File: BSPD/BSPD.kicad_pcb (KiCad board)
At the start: 2 copper layers, 100.3 x 69.5 mm, 96 parts, among them Q1 BC548, Q2 BC548, Q3 BC548, Q4 BC548, Q5 BC548, Q6 BC557, Q7 BC548, SW1 SW_DPDT_x2, U1 TL431D, U2 LM358, U3 LM358, U5 LM358, U6 4001

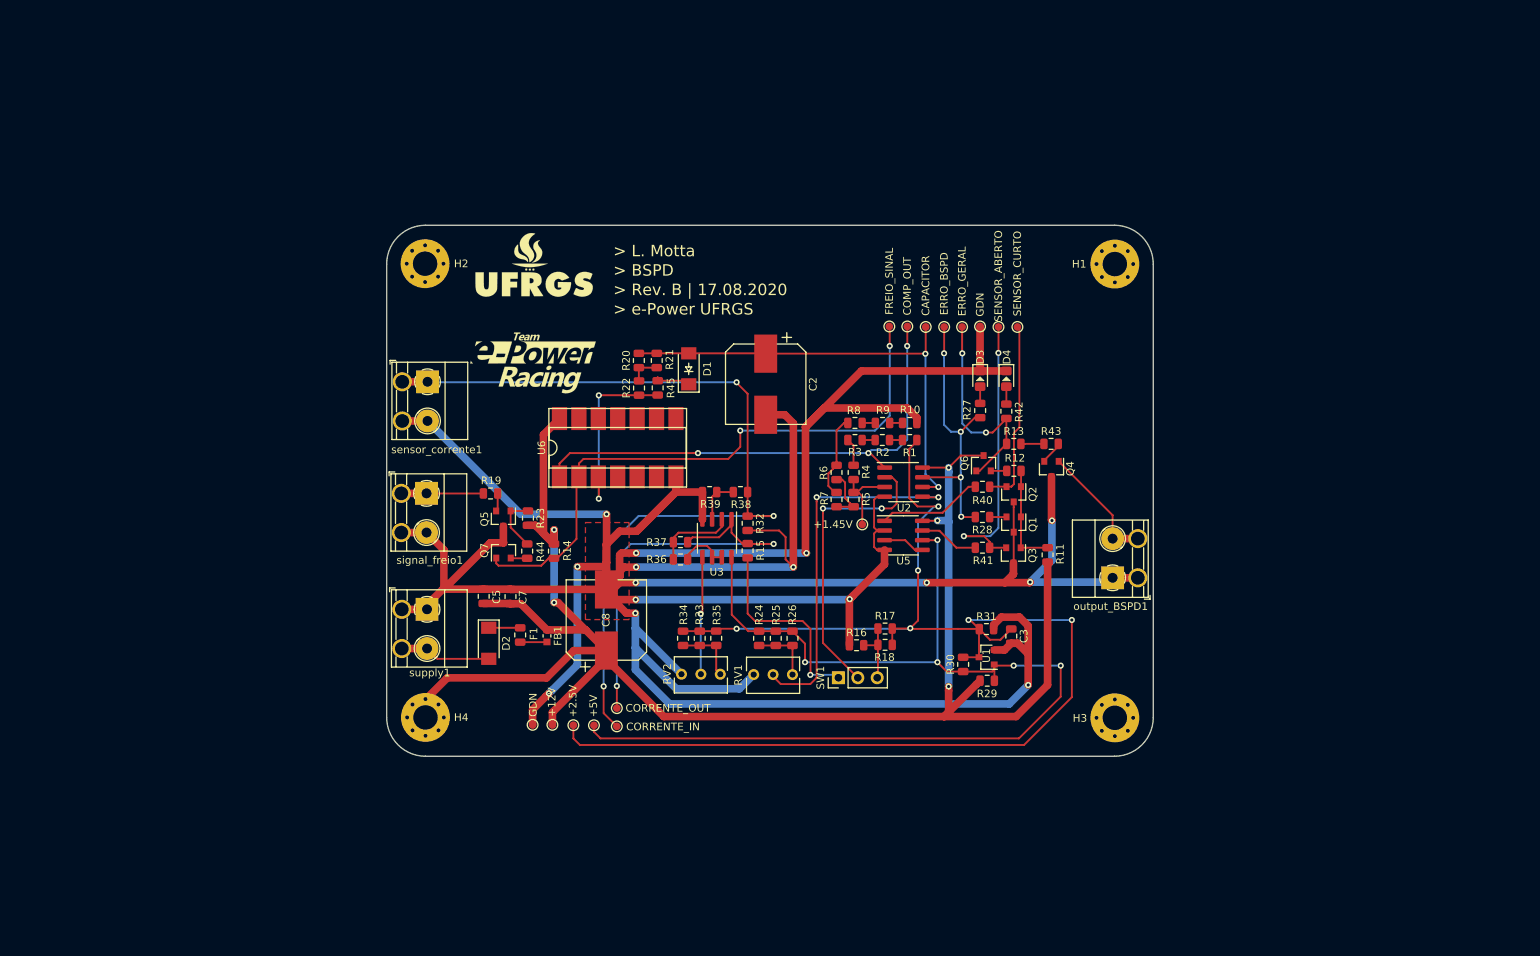
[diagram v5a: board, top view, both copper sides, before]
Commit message: BSPD atualizado e charger shutdown adicionado
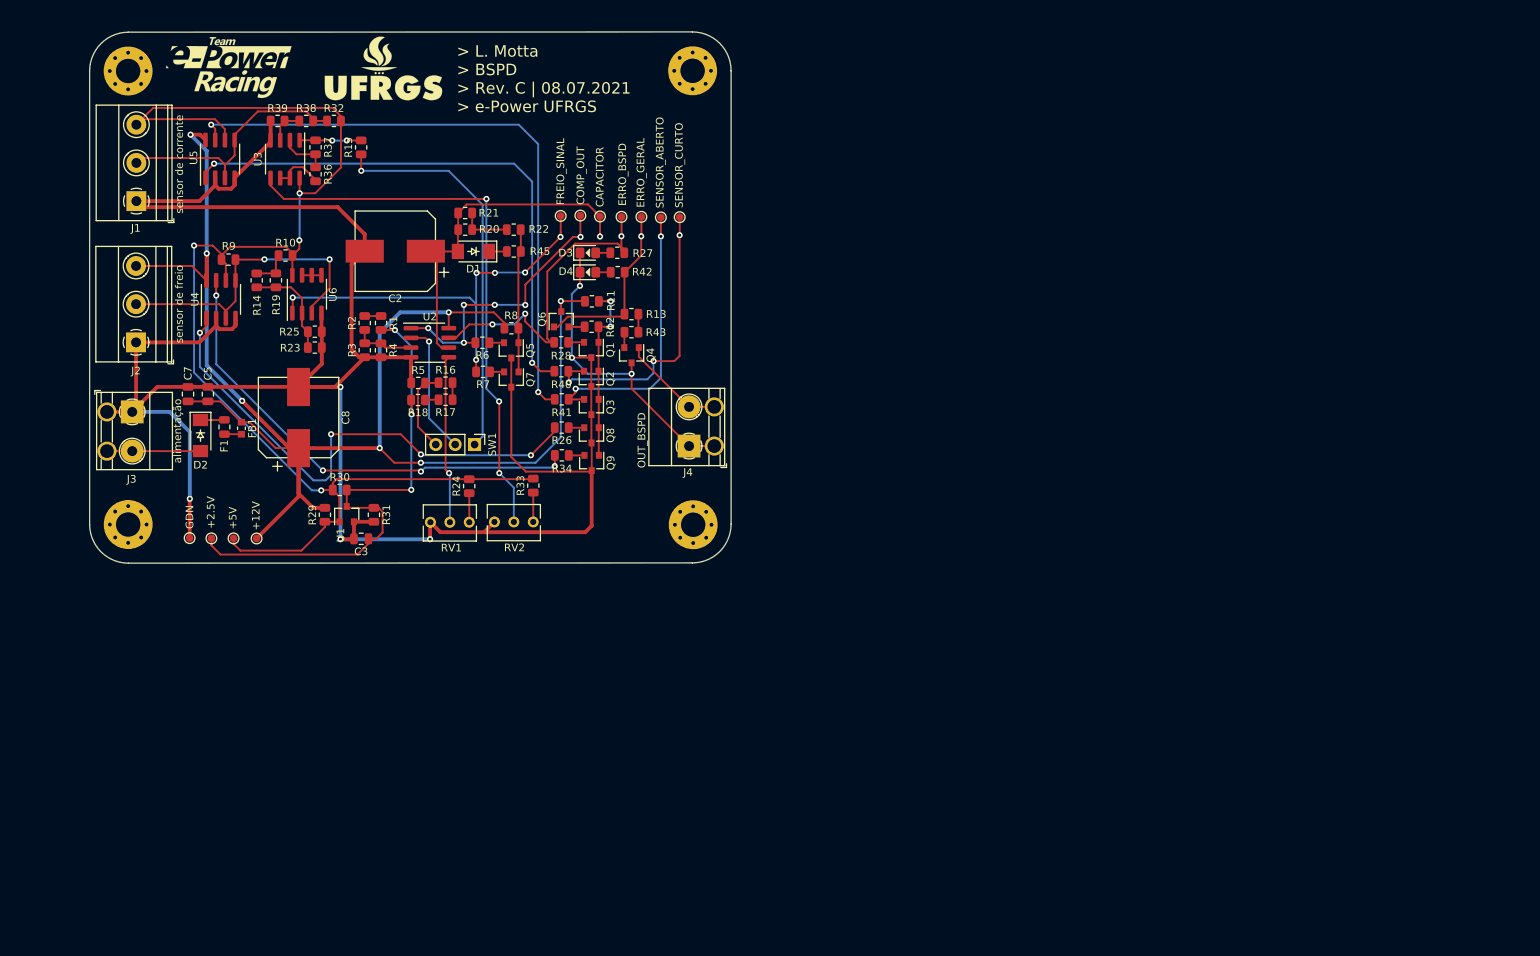
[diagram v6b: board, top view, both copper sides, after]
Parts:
- removed R35: 1k, Resistor_SMD:R_0805_2012Metric
- removed R44: 10k, Resistor_SMD:R_0805_2012Metric
- removed TP15: GDN, e-Power:TestPoint_Pad_D1.0mm
- removed TP2: +1.45V, e-Power:TestPoint_Pad_D1.0mm
- removed TP5: CORRENTE_IN, e-Power:TestPoint_Pad_D1.0mm
- removed TP6: CORRENTE_OUT, e-Power:TestPoint_Pad_D1.0mm
- removed output_BSPD1, sensor_corrente1, signal_freio1, supply1: Screw_Terminal_01x02, e-Power:TerminalBlock_Phoenix_MKDS-1,5-2_1x02_P5.08mm_Horizontal
- added J1: sensor de corrente, TerminalBlock_Phoenix:TerminalBlock_Phoenix_MKDS-1,5-3_1x03_P5.00mm_Horizontal, F.Cu at (62.0, 69.4)
- added J2: sensor de freio, TerminalBlock_Phoenix:TerminalBlock_Phoenix_MKDS-1,5-3_1x03_P5.00mm_Horizontal, F.Cu at (62.0, 87.9)
- added J3: alimentação, e-Power:TerminalBlock_Phoenix_MKDS-1,5-2_1x02_P5.08mm_Horizontal, F.Cu at (61.5, 97.0)
- added J4: OUT_BSPD, e-Power:TerminalBlock_Phoenix_MKDS-1,5-2_1x02_P5.08mm_Horizontal, F.Cu at (134.4, 101.4)
- added Q8: BC548, Package_TO_SOT_SMD:SOT-23, F.Cu at (121.6, 100.0)
- added Q9: BC548, Package_TO_SOT_SMD:SOT-23, F.Cu at (121.6, 103.7)
- added U4: LM358, Package_SO:SOIC-8_3.9x4.9mm_P1.27mm, F.Cu at (73.1, 82.2)
- R1, R14, R2, R23, R25, R26, R3, R34, R36, R38: value 1k -> 10k
- R24, R33: value 1k -> 100
- R32, R8, R9: value 10k -> 1k
- U6: value 4001 -> LM358; footprint e-Power:DIP-14-LM324 -> Package_SO:SOIC-8_3.9x4.9mm_P1.27mm
- moved U5 102.1 mm to (73.0, 63.9), turned to 90 degrees
- moved H3 101.1 mm to (134.8, 52.3)
- moved R29 89.4 mm to (86.7, 110.4), turned to 270 degrees
- moved R9 88.2 mm to (74.1, 77.0)
- moved C3 86.0 mm to (91.5, 113.6), turned to 180 degrees
- moved U1 85.8 mm to (89.6, 110.3), turned to 90 degrees
- moved R30 84.7 mm to (88.7, 107.2), turned to 0 degrees
- moved R10 84.6 mm to (81.6, 76.5), turned to 0 degrees
- moved R31 81.6 mm to (93.1, 110.4), turned to 270 degrees
- moved R32 75.5 mm to (87.9, 58.9), turned to 0 degrees
- moved U3 75.2 mm to (81.5, 63.9)
- moved R38 74.8 mm to (84.3, 58.9)
- moved R39 74.5 mm to (80.5, 58.9)
- moved R15 73.1 mm to (91.5, 62.4)
- moved R25 72.5 mm to (85.4, 86.5), turned to 180 degrees
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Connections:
- net Signal renamed Sinal
- net current_comp renamed current_comp1
- H1 pad 1: GNDREF -> Net-(H1-Pad1)
- H2 pad 1: GNDREF -> Net-(H2-Pad1)
- H3 pad 1: GNDREF -> Net-(H3-Pad1)
- H4 pad 1: +12V -> Net-(H4-Pad1)
- Q7 pad 1: Net-(Q7-Pad1) -> Net-(Q5-Pad1)
- R1 pad 1: VREF -> Net-(R1-Pad1)
- R1 pad 2: Net-(R1-Pad2) -> VREF
- R10 pad 1: GNDREF -> Net-(R10-Pad1)
- R10 pad 2: Net-(R10-Pad2) -> 5V
- R14 pad 1: Net-(Q7-Pad1) -> Net-(R14-Pad1)
- R14 pad 2: +12V -> Net-(R10-Pad1)
- R16 pad 1: GNDREF -> Net-(R16-Pad1)
- R17 pad 2: VREF -> Net-(R17-Pad2)
- R18 pad 1: Net-(R16-Pad2) -> Net-(R17-Pad2)
- R19 pad 1: Net-(Q5-Pad2) -> Net-(R14-Pad1)
- R19 pad 2: Net-(R19-Pad2) -> Net-(R10-Pad1)
- R2 pad 2: Net-(R1-Pad2) -> Net-(R1-Pad1)
- R22 pad 1: Net-(R22-Pad1) -> Net-(Q5-Pad1)
- R23 pad 1: Net-(Q5-Pad1) -> GNDREF
- R23 pad 2: +12V -> Net-(R14-Pad1)
- R25 pad 1: Net-(R24-Pad1) -> GNDREF
- R25 pad 2: 5V -> Net-(R14-Pad1)
- R26 pad 1: Net-(R24-Pad1) -> Net-(R26-Pad1)
- R26 pad 2: 5V -> freio_comp3
- R3 pad 1: Net-(R3-Pad1) -> GNDREF
- R32 pad 1: GNDREF -> sensor_corrente
- R32 pad 2: Net-(R32-Pad2) -> 5V
- R33 pad 2: VREF -> 5V
- R34 pad 1: Net-(R33-Pad1) -> Net-(R34-Pad1)
- R34 pad 2: VREF -> freio_comp4
- R38 pad 2: Net-(R32-Pad2) -> sensor_corrente
- R4 pad 1: Net-(R4-Pad1) -> GNDREF
- R4 pad 2: Net-(R3-Pad1) -> Net-(R2-Pad1)
- R45 pad 1: Net-(R22-Pad1) -> Net-(Q5-Pad1)
- R5 pad 1: Net-(R5-Pad1) -> GNDREF
- R5 pad 2: Net-(R4-Pad1) -> Net-(R16-Pad1)
- R6 pad 1: Net-(R6-Pad1) -> Net-(Q5-Pad2)
- R6 pad 2: Net-(R5-Pad1) -> Net-(R6-Pad2)
- R7 pad 1: Net-(R6-Pad1) -> Net-(Q7-Pad2)
- R7 pad 2: Net-(R5-Pad1) -> freio_press
- R8 pad 1: Net-(R8-Pad1) -> Net-(Q5-Pad1)
- R8 pad 2: Net-(R6-Pad1) -> +12V
- R9 pad 1: Net-(R10-Pad2) -> sensor_freio
- R9 pad 2: Net-(R8-Pad1) -> 5V
- SW1 pad 3: Net-(R16-Pad2) -> Net-(R16-Pad1)
- TP8 pad 1: Net-(TP8-Pad1) -> Net-(R6-Pad2)
- TP9 pad 1: Net-(Q7-Pad1) -> freio_press
- U2 pad 1: Net-(TP8-Pad1) -> Net-(R6-Pad2)
- U2 pad 3: Net-(R4-Pad1) -> Net-(R2-Pad1)
- U5 pad 3: current_out -> sensor_corrente
- U5 pad 5: current_out -> sensor_corrente
- U6 pad 1: Net-(TP8-Pad1) -> freio_press
- U6 pad 2: Net-(Q7-Pad1) -> Net-(R14-Pad1)
- U6 pad 3: Net-(R22-Pad1) -> sensor_freio
- U6 pad 4: (no net) -> GNDREF
- U6 pad 7: GNDREF -> (no net)
- U6 pad 8: (no net) -> 5V
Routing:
- net GNDREF: track 580.6 -> 347.8 mm, vias 15 -> 7
- net Net-(R32-Pad2): track 113.1 -> 0.00 mm, vias 3 -> 0
- net VREF: track 180.2 -> 69.3 mm, vias 6 -> 3
- net Net-(Q7-Pad1): track 79.0 -> 0.00 mm, vias 2 -> 0
- net Net-(R41-Pad1): track 7.86 -> 81.1 mm, vias 0 -> 2
- net Net-(R26-Pad1): track 0.00 -> 67.9 mm, vias 0 -> 4
- net Net-(TP8-Pad1): track 66.3 -> 0.00 mm, vias 3 -> 0
- net Net-(R34-Pad1): track 0.00 -> 63.0 mm, vias 0 -> 4
- net Net-(R40-Pad1): track 13.7 -> 72.0 mm, vias 0 -> 2
- net Net-(RV2-Pad2): track 15.5 -> 73.7 mm, vias 1 -> 3
- net freio_press: track 0.00 -> 55.1 mm, vias 0 -> 6
- net Sinal: track 56.2 -> 8.08 mm
- net sensor_freio: track 0.00 -> 40.7 mm, vias 0 -> 2
- net Net-(R6-Pad2): track 0.00 -> 37.5 mm, vias 0 -> 6
- net sensor_corrente: track 0.00 -> 33.2 mm
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- removed copper zone on F.Cu, net GNDREF
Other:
- board size 100.3 x 69.5 mm -> 84 x 69.5 mm
- board text added: "> L. Motta > BSPD > Rev. C | 08.07.2021 > e-Power UFRGS"
- board text removed: "> BSPD"
- board text removed: "> L. Motta"
- board text removed: "> Rev. B | 17.08.2020"
- board text removed: "> e-Power UFRGS"
